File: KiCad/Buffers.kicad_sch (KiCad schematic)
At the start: 5 parts, among them U122 74F245, U126 74F138, U127 74LS157, U130 74LS07, U402 74F08

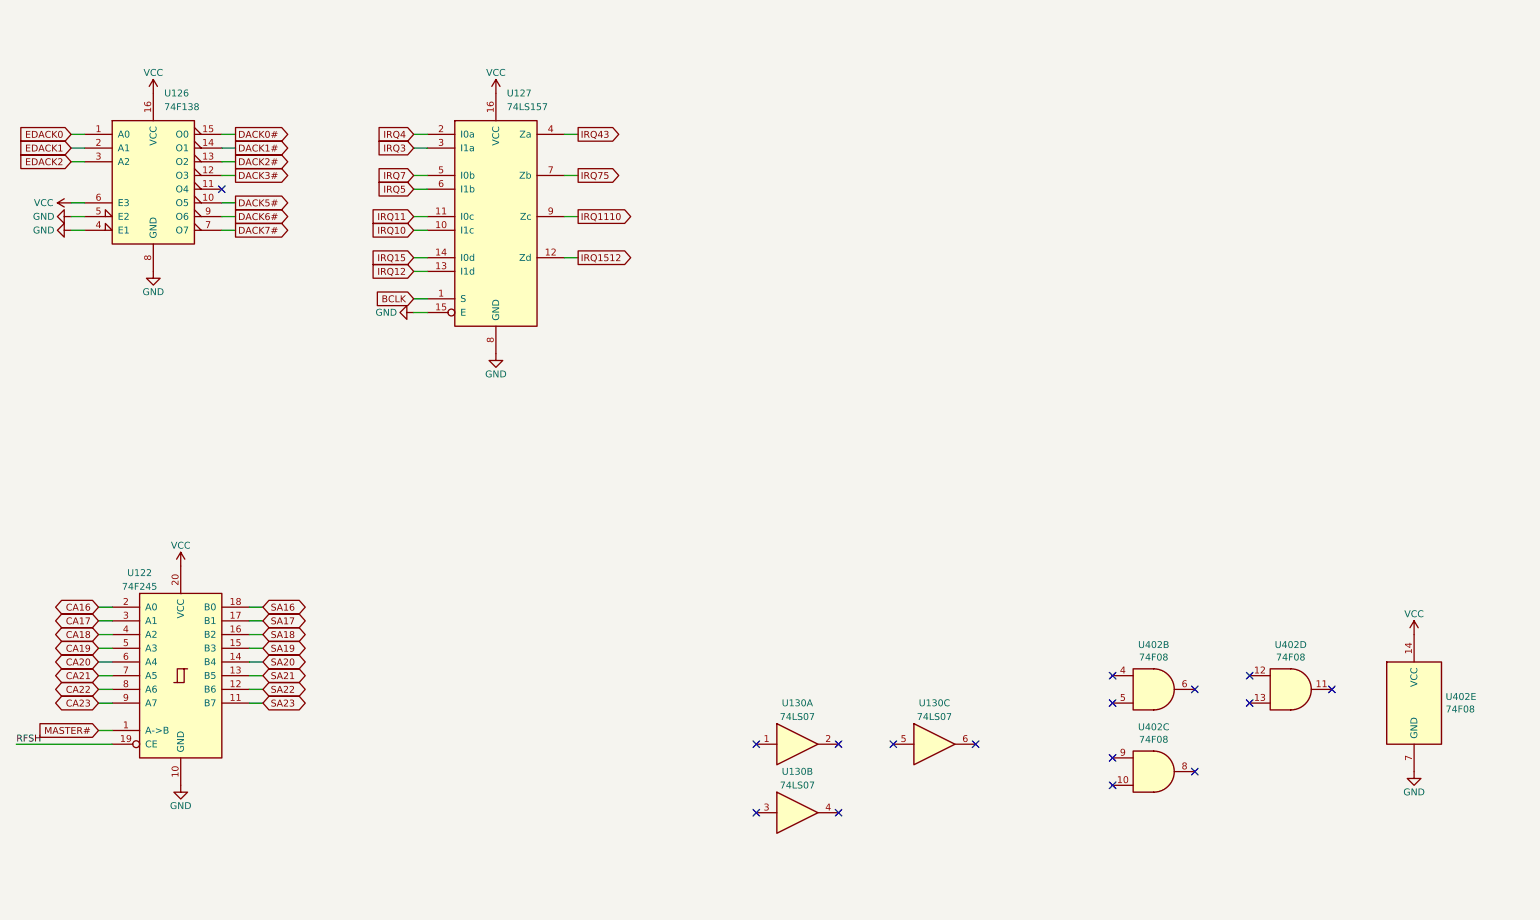
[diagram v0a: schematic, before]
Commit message: Version 0.3: Update DRAM schematic, pull-ups/pull-downs, CPU configuration jumpers
Signed-off-by: Sergey Kiselev <skiselev@gmail.com>
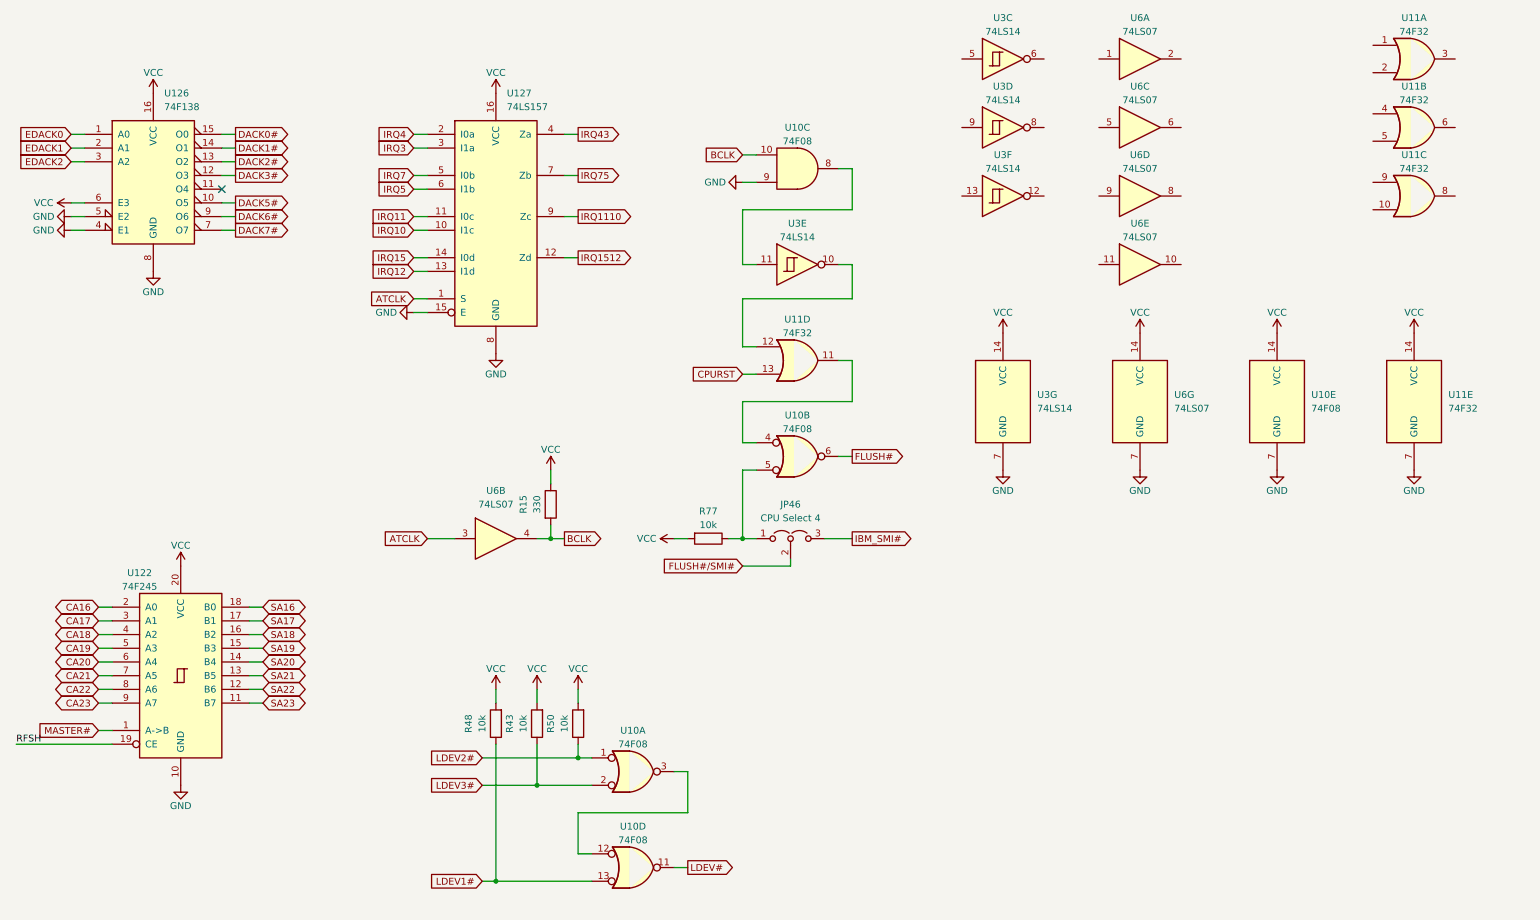
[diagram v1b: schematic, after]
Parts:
- removed U130: 74LS07, symbol 74xx:74LS07
- removed U402: 74F08, symbol 74xx:74LS08
- added JP46: CPU Select 4, symbol Jumper:Jumper_3_Open
- added R15: 330, symbol Device:R
- added R43, R48, R50, R77: 10k, symbol Device:R
- added U10: 74F08, symbol 74xx:74LS08
- added U11: 74F32, symbol 74xx:74LS32
- added U3: 74LS14, symbol 74xx:74LS14
- added U6: 74LS07, symbol 74xx:74LS07
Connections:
- net BCLK: now also R15.2, U10.10, U6.4; no longer U127.1 (S)
- net GND: now also U10.7 (GND), U10.9, U11.7 (GND), U3.7 (GND), U6.7 (GND)
- net VCC: now also R15.1, R43.2, R48.2, R50.2, R77.2, U10.14 (VCC), U11.14 (VCC), U3.14 (VCC), U6.14 (VCC)
- new net: U10.4, U11.11
- new net: U11.12, U3.10
- new net: U10.8, U3.11
- new net: U10.12, U10.3
- new net: JP46.1 (A), R77.1, U10.5
- new net ATCLK: U127.1 (S), U6.3
- new net CPURST: U11.13
- new net FLUSH#: U10.6
- new net FLUSH#/SMI#: JP46.2 (C)
- new net IBM_SMI#: JP46.3 (B)
- new net LDEV#: U10.11
- new net LDEV1#: R48.1, U10.13
- new net LDEV2#: R50.1, U10.1
- new net LDEV3#: R43.1, U10.2
- no-connect marks 16 -> 1

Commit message: Version 0.4: Update chipset connection
Signed-off-by: Sergey Kiselev <skiselev@gmail.com>
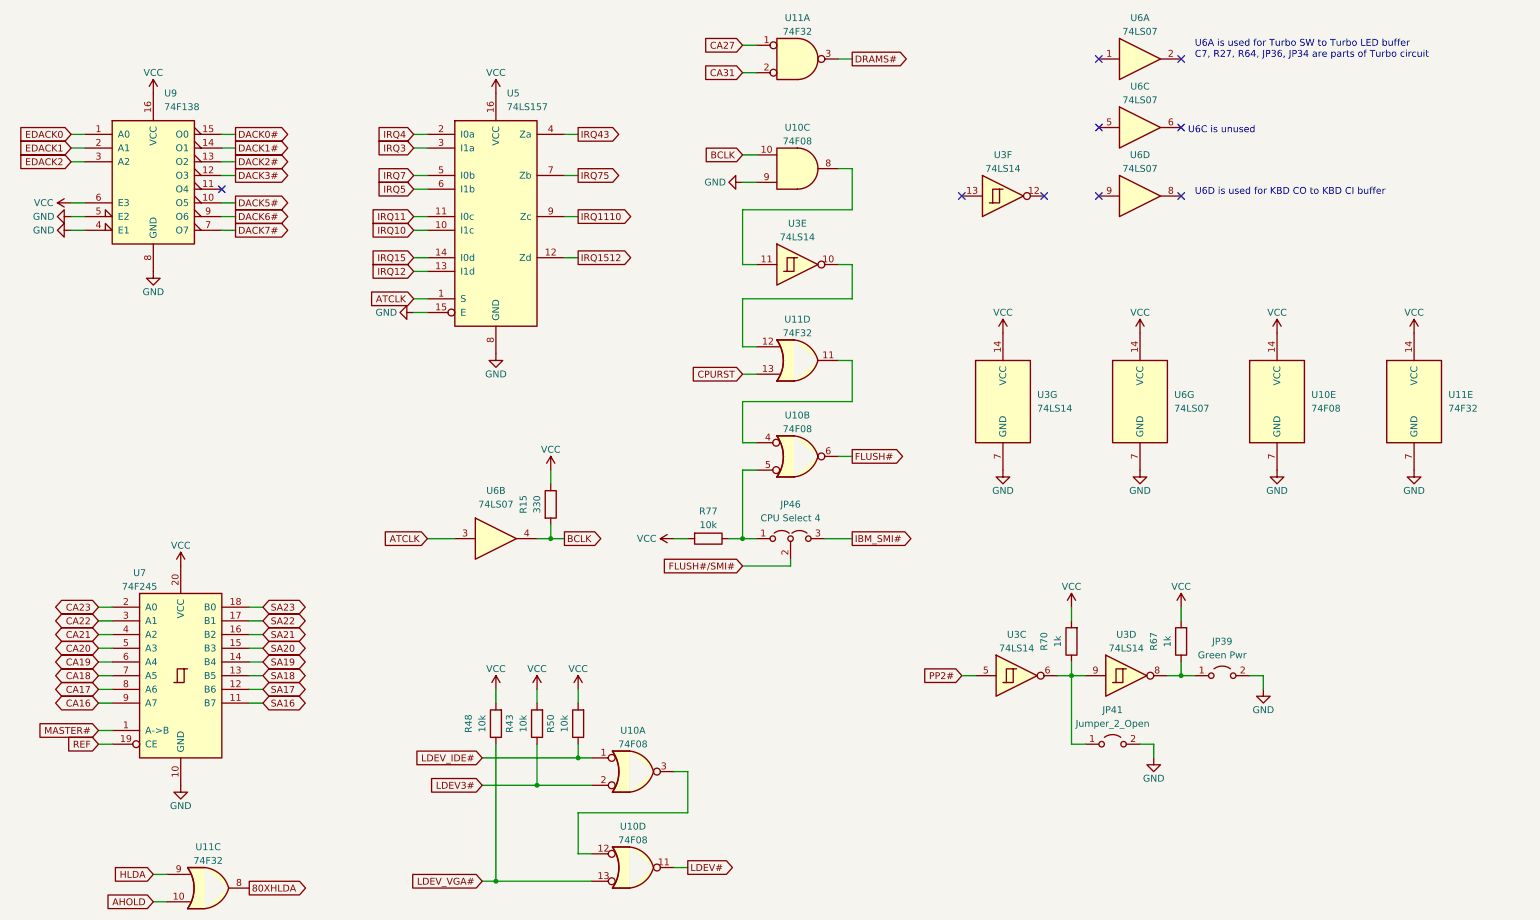
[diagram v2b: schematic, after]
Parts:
- removed unit 2 of U11
- removed unit 5 of U6
- added JP39: Green Pwr, My_Components:Conn_Pin_Header_2x1_2.54mm, symbol Jumper:Jumper_2_Open
- added JP41: Jumper_2_Open, My_Components:Conn_Pin_Header_2x1_2.54mm, symbol Jumper:Jumper_2_Open
- added R67, R70: 1k, Resistor_SMD:R_0612_1632Metric_Pad1.18x3.40mm_HandSolder, symbol Device:R
- JP46: footprint (none) -> My_Components:Conn_Pin_Header_3x1_2.54mm
- R15, R43, R48, R50, R77: footprint (none) -> Resistor_SMD:R_0612_1632Metric_Pad1.18x3.40mm_HandSolder
- U10, U11, U3, U6: footprint (none) -> My_Components:IC_DIP14_300
- U5: renamed from U127; footprint (none) -> My_Components:IC_DIP16_300
- U7: renamed from U122; footprint (none) -> My_Components:IC_DIP20_300
- U9: renamed from U126; footprint (none) -> My_Components:IC_DIP16_300
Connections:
- net CA16: now also U7.9 (A7); no longer U7.2 (A0)
- net CA17: now also U7.8 (A6); no longer U7.3 (A1)
- net CA18: now also U7.7 (A5); no longer U7.4 (A2)
- net CA19: now also U7.6 (A4); no longer U7.5 (A3)
- net CA20: now also U7.5 (A3); no longer U7.6 (A4)
- net CA21: now also U7.4 (A2); no longer U7.7 (A5)
- net CA22: now also U7.3 (A1); no longer U7.8 (A6)
- net CA23: now also U7.2 (A0); no longer U7.9 (A7)
- net GND: now also JP39.2 (B), JP41.2 (B)
- net SA16: now also U7.11 (B7); no longer U7.18 (B0)
- net SA17: now also U7.12 (B6); no longer U7.17 (B1)
- net SA18: now also U7.13 (B5); no longer U7.16 (B2)
- net SA19: now also U7.14 (B4); no longer U7.15 (B3)
- net SA20: now also U7.15 (B3); no longer U7.14 (B4)
- net SA21: now also U7.16 (B2); no longer U7.13 (B5)
- net SA22: now also U7.17 (B1); no longer U7.12 (B6)
- net SA23: now also U7.18 (B0); no longer U7.11 (B7)
- net VCC: now also R67.2, R70.2
- net AHOLD: now reaches U11.10
- net 80XHLDA: now reaches U11.8
- net HLDA: now reaches U11.9
- net at U3.8: now also JP39.1 (A), R67.1
- net at U3.9: now also U3.6, JP41.1 (A), R70.1
- net CA27: now reaches U11.1
- net CA31: now reaches U11.2
- net DRAMS#: now reaches U11.3
- net PP2#: now reaches U3.5
- net LDEV1# renamed LDEV_VGA#
- net LDEV2# renamed LDEV_IDE#
- net RFSH renamed REF
- no-connect marks 1 -> 9
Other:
- note added: "U6A is used for Turbo SW to Turbo LED buffer C7, R27, R64, JP36, JP34 are parts of Turbo circuit"
- note added: "U6C is unused"
- note added: "U6D is used for KBD CO to KBD CI buffer"
- moved on the sheet: U11C, U3C, U3D
